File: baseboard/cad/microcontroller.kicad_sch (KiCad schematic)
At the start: 12 parts, among them J16 Conn_01x04_Pin, SW3 SW_DIP_x01, U1 STM32G031K8Ux, U3 ADG5434, Y1 830054236

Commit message: finished initial layout
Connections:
- net +12V_EN: now also U1.19 (PA9/NC); no longer U1.21 (PA10/NC)
- net -12V_EN: now also U1.20 (PC6); no longer U1.22 (PA11/PA9)
- net VLED1: now also U1.9 (PA2); no longer U1.29 (PB5)
- net VLED2: now also U1.8 (PA1); no longer U1.28 (PB4)
- net V_FTSW_A: now also U1.18 (PA8); no longer U1.24 (PA13)
- net V_FTSW_B: now also U1.17 (PB2); no longer U1.23 (PA12/PA10)
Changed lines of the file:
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@@
   (junction (at 66.04 158.75) (diameter 0) (color 0 0 0 0)
   )
-  (no_connect (at 115.57 104.14))
+  (no_connect (at 87.63 111.76))
   (no_connect (at 87.63 99.06))
-  (no_connect (at 115.57 86.36))
-  (no_connect (at 87.63 104.14))
-  (no_connect (at 115.57 88.9))
+  (no_connect (at 115.57 116.84))
+  (no_connect (at 115.57 114.3))
   (no_connect (at 115.57 83.82))
+  (no_connect (at 115.57 109.22))
   (no_connect (at 87.63 114.3))
-  (no_connect (at 87.63 88.9))
+  (no_connect (at 87.63 109.22))
   (no_connect (at 87.63 121.92))
   (no_connect (at 87.63 106.68))
+  (no_connect (at 115.57 111.76))
   (no_connect (at 87.63 101.6))
   (no_connect (at 115.57 119.38))
-  (no_connect (at 115.57 106.68))
   (no_connect (at 115.57 121.92))
   (wire (pts (xy 58.42 163.83) (xy 44.45 163.83))
@@
     (effects (font (size 1.27 1.27)) (justify left bottom))
   )
-  (global_label "-12V_EN" (shape output) (at 115.57 111.76 0) (fields_autoplaced)
-    (effects (font (size 1.27 1.27)) (justify left))
-    (property "Intersheetrefs" "${INTERSHEET_REFS}" (at 125.7934 111.76 0)
-      (effects (font (size 1.27 1.27)) (justify left) hide)
-    )
-  )
-  (global_label "+12V_EN" (shape output) (at 115.57 109.22 0) (fields_autoplaced)
-    (effects (font (size 1.27 1.27)) (justify left))
-    (property "Intersheetrefs" "${INTERSHEET_REFS}" (at 125.7934 109.22 0)
-      (effects (font (size 1.27 1.27)) (justify left) hide)
-    )
-  )
   (global_label "AUDIO_IN_A" (shape output) (at 193.04 49.53 0) (fields_autoplaced)
     (effects (font (size 1.27 1.27)) (justify left))
@@
     )
   )
-  (global_label "V_FTSW_A" (shape input) (at 115.57 116.84 0) (fields_autoplaced)
-    (effects (font (size 1.27 1.27)) (justify left))
-    (property "Intersheetrefs" "${INTERSHEET_REFS}" (at 126.8126 116.7606 0)
-      (effects (font (size 1.27 1.27)) (justify left) hide)
-    )
-  )
   (global_label "AUDIO_IN_FILT" (shape input) (at 157.48 52.07 180) (fields_autoplaced)
     (effects (font (size 1.27 1.27)) (justify right))
@@
     )
   )
-  (global_label "VLED1" (shape output) (at 87.63 111.76 180) (fields_autoplaced)
-    (effects (font (size 1.27 1.27)) (justify right))
-    (property "Intersheetrefs" "${INTERSHEET_REFS}" (at 79.5382 111.76 0)
-      (effects (font (size 1.27 1.27)) (justify right) hide)
-    )
-  )
-  (global_label "VLED2" (shape output) (at 87.63 109.22 180) (fields_autoplaced)
-    (effects (font (size 1.27 1.27)) (justify right))
-    (property "Intersheetrefs" "${INTERSHEET_REFS}" (at 79.5382 109.22 0)
-      (effects (font (size 1.27 1.27)) (justify right) hide)
+  (global_label "+12V_EN" (shape output) (at 115.57 106.68 0) (fields_autoplaced)
+    (effects (font (size 1.27 1.27)) (justify left))
+    (property "Intersheetrefs" "${INTERSHEET_REFS}" (at 125.7934 106.68 0)
+      (effects (font (size 1.27 1.27)) (justify left) hide)
+    )
+  )
+  (global_label "V_FTSW_A" (shape input) (at 115.57 104.14 0) (fields_autoplaced)
+    (effects (font (size 1.27 1.27)) (justify left))
+    (property "Intersheetrefs" "${INTERSHEET_REFS}" (at 126.8126 104.0606 0)
+      (effects (font (size 1.27 1.27)) (justify left) hide)
     )
   )
@@
     )
   )
+  (global_label "VLED1" (shape output) (at 115.57 88.9 0) (fields_autoplaced)
+    (effects (font (size 1.27 1.27)) (justify left))
+    (property "Intersheetrefs" "${INTERSHEET_REFS}" (at 123.6618 88.9 0)
+      (effects (font (size 1.27 1.27)) (justify left) hide)
+    )
+  )
   (global_label "SWDCK" (shape bidirectional) (at 96.52 171.45 0) (fields_autoplaced)
     (effects (font (size 1.27 1.27)) (justify left))
@@
     )
   )
-  (global_label "V_FTSW_B" (shape input) (at 115.57 114.3 0) (fields_autoplaced)
-    (effects (font (size 1.27 1.27)) (justify left))
-    (property "Intersheetrefs" "${INTERSHEET_REFS}" (at 126.9941 114.2206 0)
+  (global_label "VLED2" (shape output) (at 115.57 86.36 0) (fields_autoplaced)
+    (effects (font (size 1.27 1.27)) (justify left))
+    (property "Intersheetrefs" "${INTERSHEET_REFS}" (at 123.6618 86.36 0)
       (effects (font (size 1.27 1.27)) (justify left) hide)
     )
@@
     )
   )
+  (global_label "V_FTSW_B" (shape input) (at 87.63 104.14 180) (fields_autoplaced)
+    (effects (font (size 1.27 1.27)) (justify right))
+    (property "Intersheetrefs" "${INTERSHEET_REFS}" (at 76.2059 104.0606 0)
+      (effects (font (size 1.27 1.27)) (justify right) hide)
+    )
+  )
   (global_label "AUDIO_OUT_FILT" (shape output) (at 146.05 82.55 180) (fields_autoplaced)
     (effects (font (size 1.27 1.27)) (justify right))
@@
       (effects (font (size 1.27 1.27)) (justify right) hide)
     )
+  )
+  (global_label "-12V_EN" (shape output) (at 87.63 88.9 180) (fields_autoplaced)
+    (effects (font (size 1.27 1.27)) (justify right))
+    (property "Intersheetrefs" "${INTERSHEET_REFS}" (at 77.4066 88.9 0)
+      (effects (font (size 1.27 1.27)) (justify right) hide)
+    )

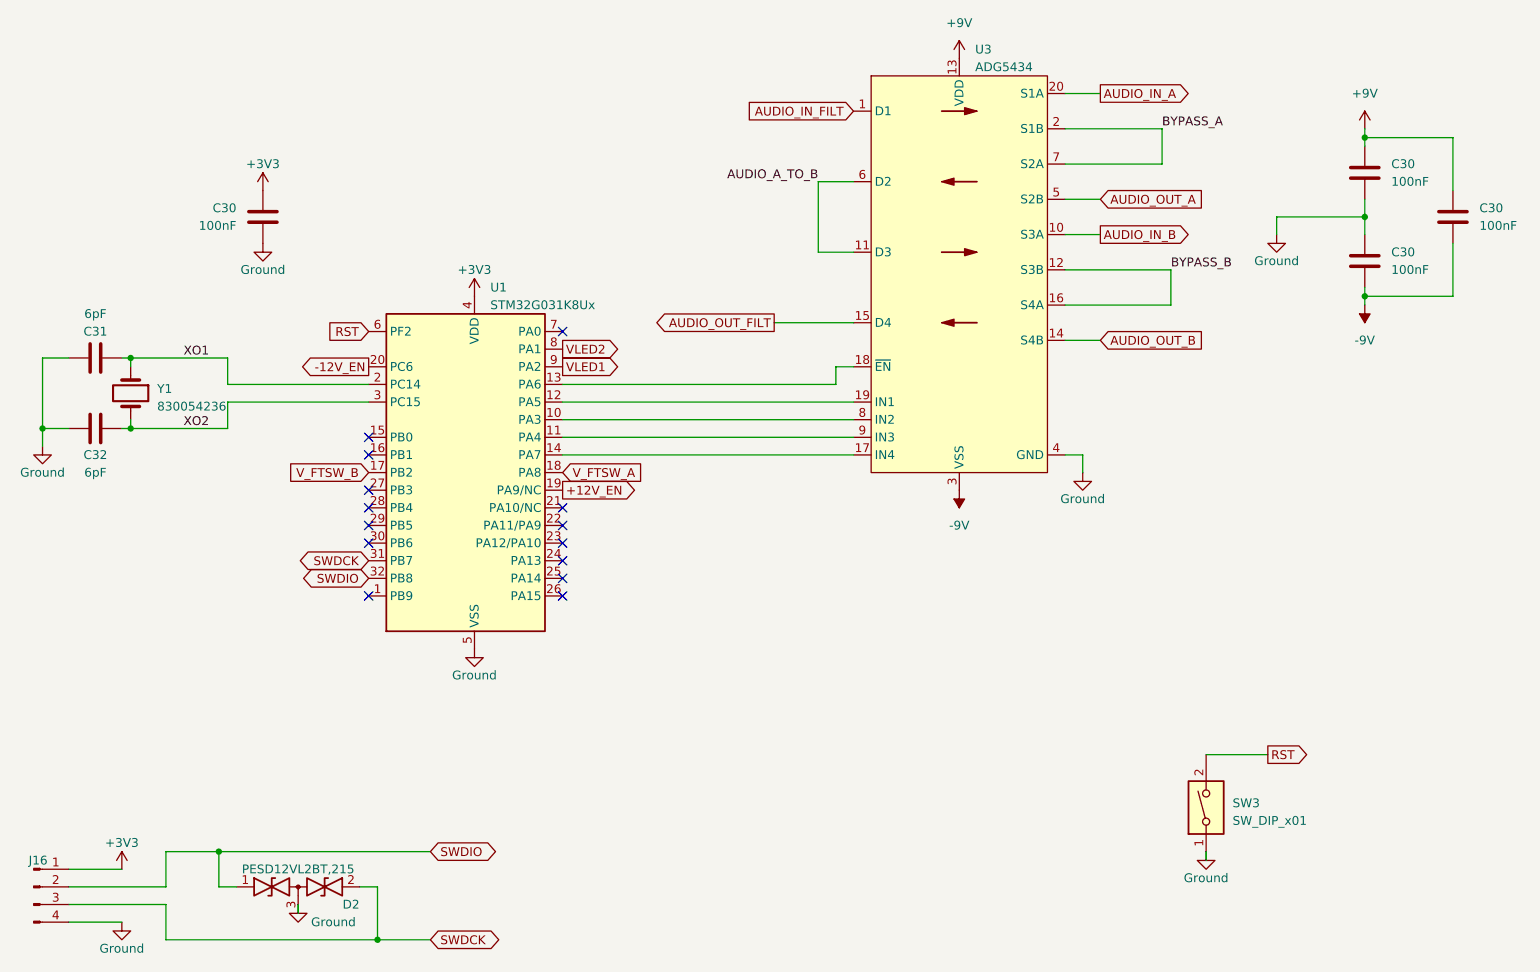
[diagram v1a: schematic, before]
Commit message: cleaning up layout, added graphic symbols
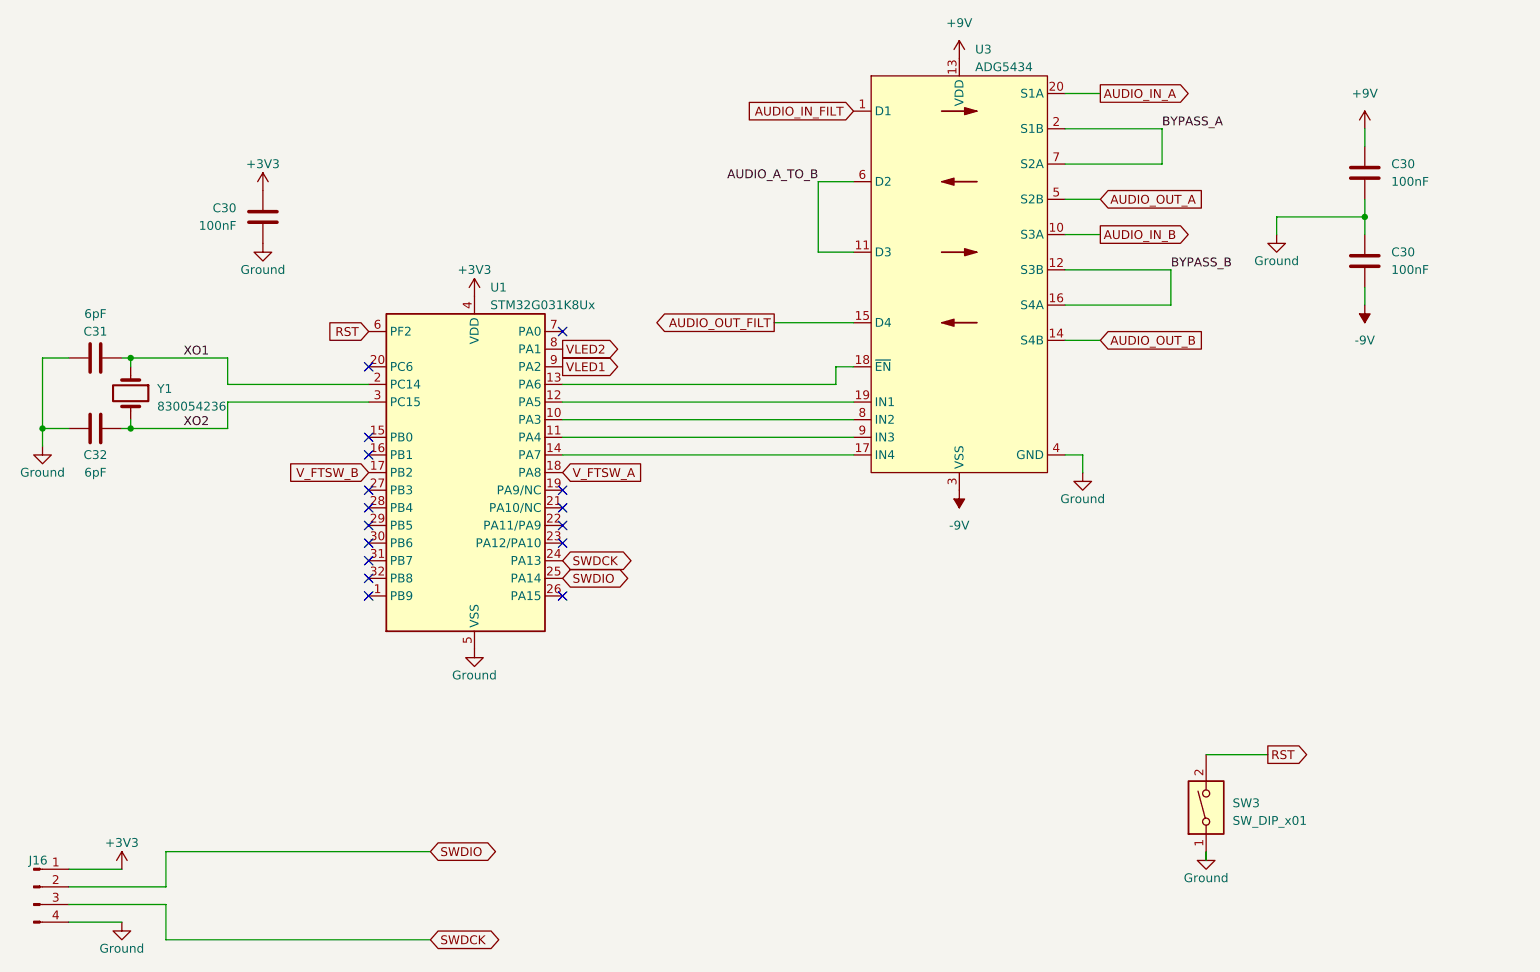
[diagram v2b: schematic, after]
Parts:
- removed C30: 100nF, Capacitor_SMD:C_1206_3216Metric, symbol Device:C
- removed D2: PESD12VL2BT,215, Package_TO_SOT_SMD:SOT-23, symbol Library:PESD12VL2BT,215
- J16: footprint Connector_PinHeader_2.54mm:PinHeader_1x04_P2.54mm_Vertical -> Connector_PinHeader_2.54mm:PinHeader_2x02_P2.54mm_Vertical_SMD
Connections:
- net SWDCK: now also U1.24 (PA13); no longer U1.31 (PB7)
- net SWDIO: now also U1.25 (PA14); no longer U1.32 (PB8)
- net +12V_EN: no longer names the net of U1.19 (PA9/NC)
- net -12V_EN: no longer names the net of U1.20 (PC6)
- no-connect marks 14 -> 16
